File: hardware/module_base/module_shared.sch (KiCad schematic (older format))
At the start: 5 parts, among them J1 RJ45_LED_Shielded, U1 WAVGAT_CAN

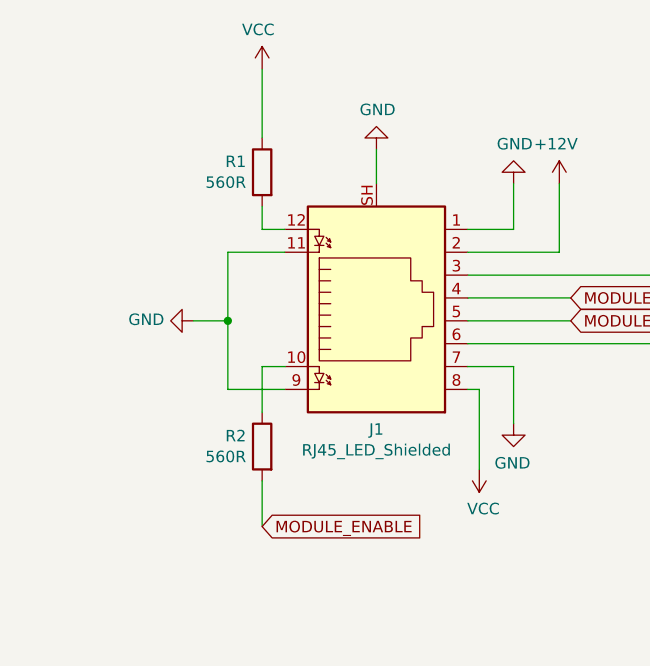
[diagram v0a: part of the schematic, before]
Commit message: ModuleBase PCB: change RJ45 jack, add mounting holes, reorganize
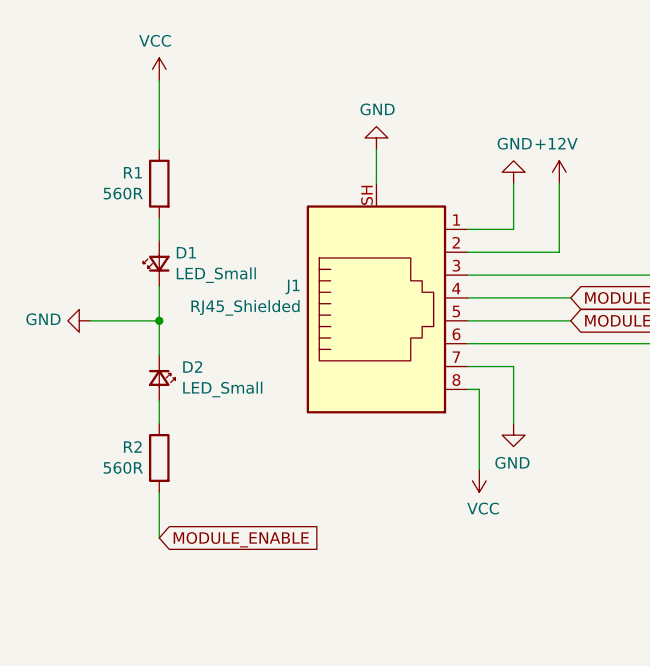
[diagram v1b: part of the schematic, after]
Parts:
- removed J1: RJ45_LED_Shielded, Connector_RJ:RJ45_Amphenol_RJHSE538X, symbol Connector:RJ45_LED_Shielded
- added D1, D2: LED_Small, LED_THT:LED_D3.0mm, symbol Device:LED_Small
- added J1: RJ45_Shielded, RJ45_5224:RJ45_5224, symbol Connector:RJ45_Shielded
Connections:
- net +12V: now also J1.2
- net GND: now also D1.1 (K), D2.1 (K), J1.1, J1.7, J1.SH
- net MODULE_ENABLE: now also J1.5
- net MODULE_READY: now also J1.4
- net VCC: now also J1.8
- net at U1.J3_1 (CAN_L): now also J1.3
- net at U1.J3_2 (CAN_H): now also J1.6
- net at R2.1: now also D2.2 (A)
- net at R1.2: now also D1.2 (A)
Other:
- moved on the sheet: R1, R2

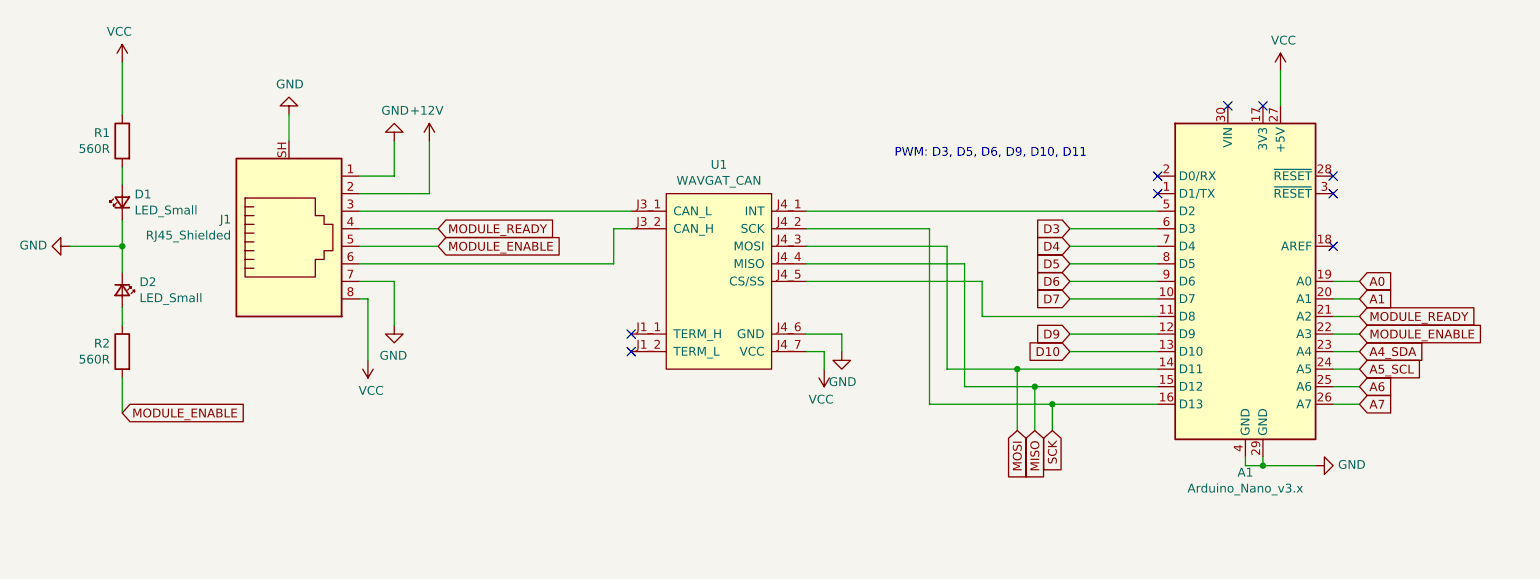
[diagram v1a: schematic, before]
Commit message: ModuleBase PCB: expose Arduino pins + SPI + more GND/5V
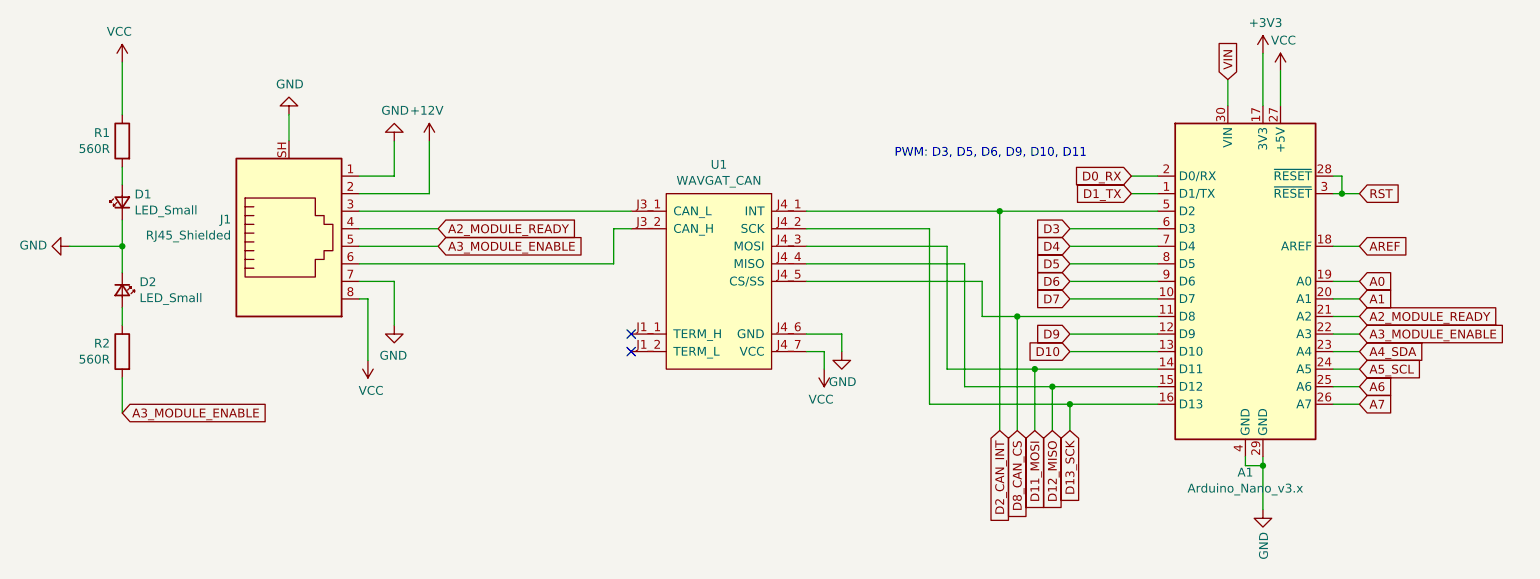
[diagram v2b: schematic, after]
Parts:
- R1, R2: footprint Resistor_SMD:R_0603_1608Metric_Pad1.05x0.95mm_HandSolder -> Resistor_SMD:R_0603_1608Metric_Pad0.98x0.95mm_HandSolder
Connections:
- net D2_CAN_INT: now reaches A1.5 (D2), U1.J4_1 (INT)
- net D8_CAN_CS: now reaches A1.11 (D8), U1.J4_5 (CS/SS)
- net D1_TX: now reaches A1.1 (D1/TX)
- net +3V3: now reaches A1.17 (3V3)
- net AREF: now reaches A1.18 (AREF)
- net D0_RX: now reaches A1.2 (D0/RX)
- net RST: now reaches A1.28 (~RESET)
- net RST: now also A1.3 (~RESET)
- net VIN: now reaches A1.30 (VIN)
- net MISO renamed D12_MISO
- net MODULE_ENABLE renamed A3_MODULE_ENABLE
- net MODULE_READY renamed A2_MODULE_READY
- net MOSI renamed D11_MOSI
- net SCK renamed D13_SCK
- no-connect marks 9 -> 2
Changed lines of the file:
@@
 	8750 3300 8600 3300
 Text GLabel 8750 3600 2    50   Input ~ 0
-MODULE_ENABLE
+A3_MODULE_ENABLE
 Text GLabel 8750 3400 2    50   Input ~ 0
 A1
@@
 D5
 Wire Wire Line
-	6800 3800 6400 3800
-Wire Wire Line
-	6800 4150 6800 3800
-Wire Wire Line
-	6900 3900 7600 3900
-Wire Wire Line
-	6900 4150 6900 3900
-Wire Wire Line
-	7000 4000 6300 4000
-Wire Wire Line
-	7000 4150 7000 4000
+	7100 4150 7100 4000
+Text GLabel 7100 4150 3    50   Input ~ 0
+D13_SCK
 Text GLabel 7000 4150 3    50   Input ~ 0
-SCK
+D12_MISO
 Text GLabel 6900 4150 3    50   Input ~ 0
-MISO
-Text GLabel 6800 4150 3    50   Input ~ 0
-MOSI
+D11_MOSI
 Text GLabel 8750 3800 2    50   Input ~ 0
 A5_SCL
@@
 	3500 3100 3050 3100
 Text GLabel 3500 3100 2    50   Input ~ 0
-MODULE_ENABLE
+A3_MODULE_ENABLE
 Wire Wire Line
 	8200 4350 8100 4350
@@
 Wire Wire Line
 	8100 4350 8100 4300
-Connection ~ 8200 4350
-Wire Wire Line
-	8500 4350 8200 4350
 $Comp
 L power:GND #PWR?
 U 1 1 5F2CBDF9
-P 8500 4350
+P 8200 4600
 AR Path="/5F2CBDF9" Ref="#PWR?"  Part="1"
 AR Path="/5EF969E2/5F2CBDF9" Ref="#PWR011"  Part="1"
@@
 AR Path="/5F72C2C1/5F2CBDF9" Ref="#PWR?"  Part="1"
 AR Path="/5F6EA359/5F2CBDF9" Ref="#PWR011"  Part="1"
-F 0 "#PWR011" H 8500 4100 50  0001 C CNN
-F 1 "GND" V 8505 4222 50  0000 R CNN
-F 2 "" H 8500 4350 50  0001 C CNN
-F 3 "" H 8500 4350 50  0001 C CNN
-	1    8500 4350
-	0    -1   -1   0
+F 0 "#PWR011" H 8200 4350 50  0001 C CNN
+F 1 "GND" V 8205 4472 50  0000 R CNN
+F 2 "" H 8200 4600 50  0001 C CNN
+F 3 "" H 8200 4600 50  0001 C CNN
+	1    8200 4600
+	1    0    0    -1
 $EndComp
 Wire Wire Line
@@
 F 0 "R2" H 1770 3746 50  0000 L CNN
 F 1 "560R" H 1770 3655 50  0000 L CNN
-F 2 "Resistor_SMD:R_0603_1608Metric_Pad1.05x0.95mm_HandSolder" V 1630 3700 50  0001 C CNN
+F 2 "Resistor_SMD:R_0603_1608Metric_Pad0.98x0.95mm_HandSolder" V 1630 3700 50  0001 C CNN
 F 3 "~" H 1700 3700 50  0001 C CNN
 	1    1700 3700
@@
 F 0 "R1" H 1770 2546 50  0000 L CNN
 F 1 "560R" H 1770 2455 50  0000 L CNN
-F 2 "Resistor_SMD:R_0603_1608Metric_Pad1.05x0.95mm_HandSolder" V 1630 2500 50  0001 C CNN
+F 2 "Resistor_SMD:R_0603_1608Metric_Pad0.98x0.95mm_HandSolder" V 1630 2500 50  0001 C CNN
 F 3 "~" H 1700 2500 50  0001 C CNN
 	1    1700 2500
@@
 Wire Wire Line
 	6500 3200 6500 3900
-Connection ~ 6900 3900
-Wire Wire Line
-	6500 3900 6900 3900
 Wire Wire Line
 	5600 3200 6500 3200
@@
 Wire Wire Line
 	6400 3800 6400 3100
-Connection ~ 6800 3800
-Wire Wire Line
-	7600 3800 6800 3800
+Wire Wire Line
+	7600 3800 6900 3800
 Wire Wire Line
 	6300 3000 5600 3000
 Wire Wire Line
 	6300 4000 6300 3000
-Connection ~ 7000 4000
-Wire Wire Line
-	7600 4000 7000 4000
+Wire Wire Line
+	7600 4000 7100 4000
 $Comp
 L power:GND #PWR?
@@
 $EndComp
 Wire Wire Line
-	5600 2900 7600 2900
+	5600 2900 6700 2900
 Text GLabel 8750 3500 2    50   Input ~ 0
-MODULE_READY
+A2_MODULE_READY
 NoConn ~ 4600 3600
 NoConn ~ 4600 3700
-NoConn ~ 7600 2800
-NoConn ~ 7600 2700
-NoConn ~ 8000 2300
-NoConn ~ 8200 2300
-NoConn ~ 8600 3100
-NoConn ~ 8600 2800
-NoConn ~ 8600 2700
 Wire Wire Line
 	7100 3700 7600 3700
 Wire Wire Line
 	6600 3300 6600 3500
-Wire Wire Line
-	6600 3500 7600 3500
 Text GLabel 3500 3000 2    50   Input ~ 0
-MODULE_READY
+A2_MODULE_READY
 Text GLabel 7100 3100 0    50   Input ~ 0
 D4
@@
 	2650 2350 2650 2500
 Text GLabel 1700 4050 2    50   Input ~ 0
-MODULE_ENABLE
+A3_MODULE_ENABLE
 Wire Wire Line
 	1700 2050 1700 2350
@@
 	0    1    1    0
 $EndComp
+Text GLabel 8750 2800 2    50   Input ~ 0
+RST
+Wire Wire Line
+	8750 2800 8650 2800
+Wire Wire Line
+	8650 2800 8650 2700
+Wire Wire Line
+	8650 2700 8600 2700
+Connection ~ 8650 2800
+Wire Wire Line
+	8650 2800 8600 2800
+Text GLabel 8750 3100 2    50   Input ~ 0
+AREF
+Wire Wire Line
+	8750 3100 8600 3100
+Text GLabel 7450 2700 0    50   Input ~ 0
+D0_RX
+Text GLabel 7450 2800 0    50   Input ~ 0
+D1_TX
+Wire Wire Line
+	7450 2800 7600 2800
+Wire Wire Line
+	7600 2700 7450 2700
+$Comp
+L power:+3V3 #PWR0108
+U 1 1 5FF81BB7
+P 8200 2000
+F 0 "#PWR0108" H 8200 1850 50  0001 C CNN
+F 1 "+3V3" H 8215 2173 50  0000 C CNN
+F 2 "" H 8200 2000 50  0001 C CNN
+F 3 "" H 8200 2000 50  0001 C CNN
+	1    8200 2000
+	1    0    0    -1
+$EndComp
+Text GLabel 8000 2150 1    50   Input ~ 0
+VIN
+Wire Wire Line
+	8000 2150 8000 2300
+Wire Wire Line
+	8200 2300 8200 2000
+Wire Wire Line
+	8200 4600 8200 4350
+Connection ~ 8200 4350
+Text GLabel 6800 4150 3    50   Input ~ 0
+D8_CAN_CS
+Connection ~ 6800 3500
+Wire Wire Line
+	6800 3500 7600 3500
+Connection ~ 6900 3800
+Connection ~ 7000 3900
+Wire Wire Line
+	7000 3900 7600 3900
+Connection ~ 7100 4000
+Wire Wire Line
+	6600 3500 6800 3500
+Wire Wire Line
+	6400 3800 6900 3800
+Wire Wire Line
+	6800 3500 6800 4150
+Wire Wire Line
+	6900 3800 6900 4150
+Wire Wire Line
+	6500 3900 7000 3900
+Wire Wire Line
+	7000 3900 7000 4150
+Wire Wire Line
+	6300 4000 7100 4000
+Text GLabel 6700 4150 3    50   Input ~ 0
+D2_CAN_INT
+Wire Wire Line
+	6700 4150 6700 2900
+Connection ~ 6700 2900
+Wire Wire Line
+	6700 2900 7600 2900
 $EndSCHEMATC
